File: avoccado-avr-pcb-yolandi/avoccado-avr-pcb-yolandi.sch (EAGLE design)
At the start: 55 parts, among them Q1 16MHz, Q2 FET, U2 MCP73831

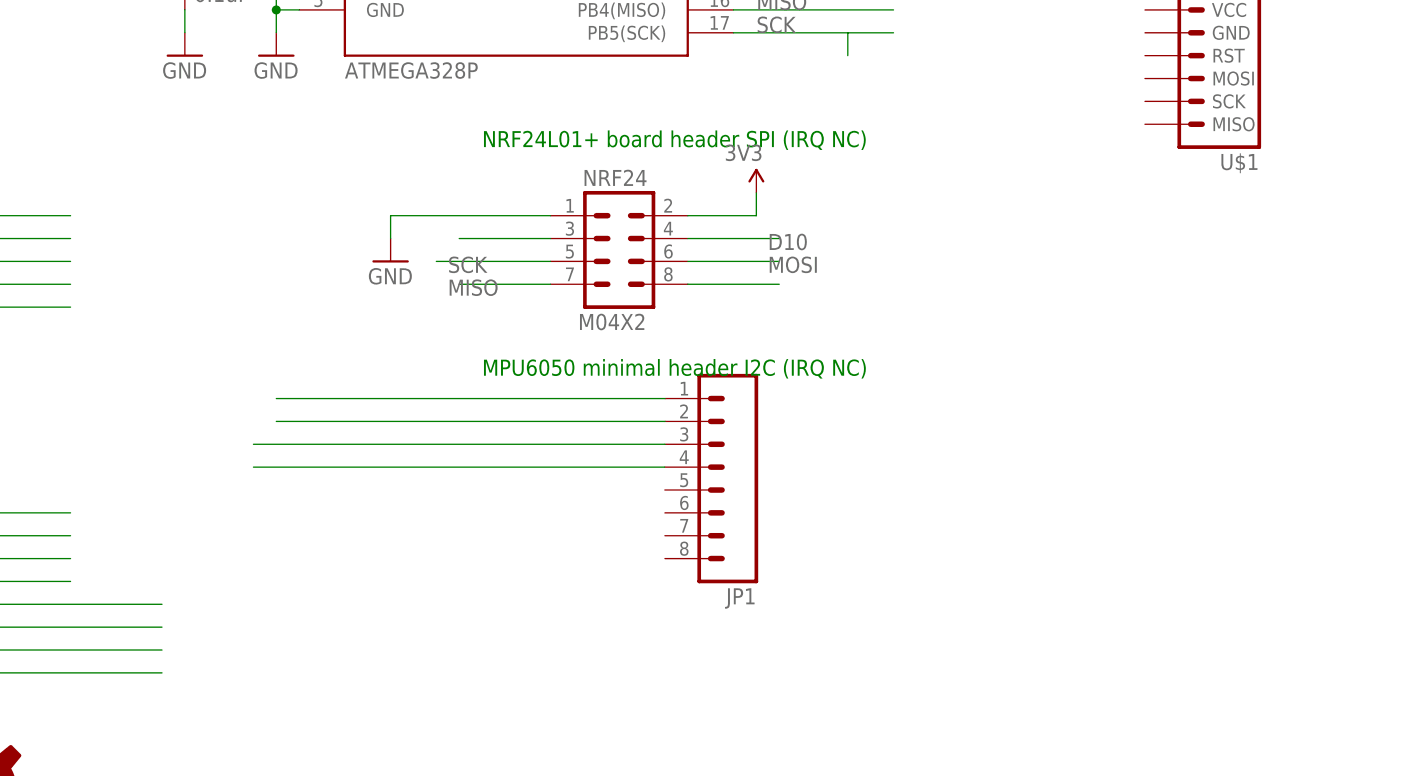
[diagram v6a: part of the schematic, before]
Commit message: change pkg of NRF24 header to round pins
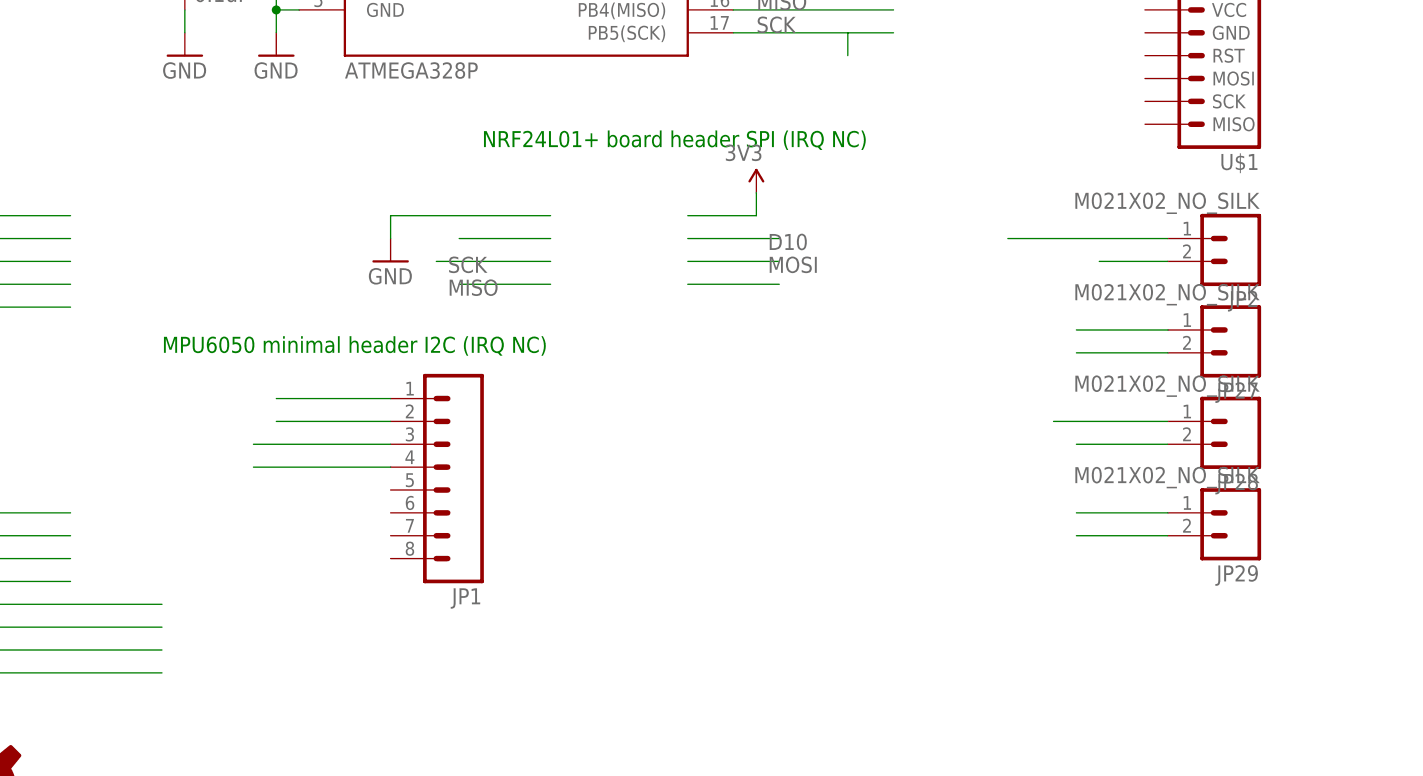
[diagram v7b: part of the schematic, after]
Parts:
- removed NRF24: M04X2, SparkFun-Connectors:M04X2
- added JP2, JP27, JP28, JP29: M021X02_NO_SILK, SparkFun-Connectors:M021X02_NO_SILK
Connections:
- net 3V3: now also JP2.2; no longer NRF24.2
- net A7: now also JP29.2; no longer NRF24.8
- net D10: now also JP27.2; no longer NRF24.4
- net D9: now also JP27.1; no longer NRF24.3
- net GND: now also JP2.1; no longer NRF24.1
- net MISO: now also JP29.1; no longer NRF24.7
- net MOSI: now also JP28.2; no longer NRF24.6
- net SCK: now also JP28.1; no longer NRF24.5
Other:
- moved on the sheet: JP1
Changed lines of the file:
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@@
 <part name="GND9" library="SparkFun" deviceset="GND" device=""/>
 <part name="R5" library="SparkFun-Resistors" deviceset="RESISTOR" device="0603" value="1M"/>
-<part name="NRF24" library="SparkFun-Connectors" deviceset="M04X2" device=""/>
 <part name="GND10" library="SparkFun" deviceset="GND" device=""/>
 <part name="P+2" library="SparkFun" deviceset="3.3V" device="" value="3V3"/>
@@
 <part name="JP25" library="SparkFun-Connectors" deviceset="M01" device="POGOPIN_HOLE_0.58"/>
 <part name="JP26" library="SparkFun-Connectors" deviceset="M01" device="POGOPIN_HOLE_0.58"/>
+<part name="JP2" library="SparkFun-Connectors" deviceset="M02" device="1X02_NO_SILK"/>
+<part name="JP27" library="SparkFun-Connectors" deviceset="M02" device="1X02_NO_SILK"/>
+<part name="JP28" library="SparkFun-Connectors" deviceset="M02" device="1X02_NO_SILK"/>
+<part name="JP29" library="SparkFun-Connectors" deviceset="M02" device="1X02_NO_SILK"/>
 </parts>
 <sheets>
@@
 <plain>
 <text x="187.96" y="83.82" size="1.778" layer="91">NRF24L01+ board header SPI (IRQ NC)</text>
-<text x="187.96" y="58.42" size="1.778" layer="91">MPU6050 minimal header I2C (IRQ NC)</text>
+<text x="152.4" y="60.96" size="1.778" layer="91">MPU6050 minimal header I2C (IRQ NC)</text>
 <text x="175.26" y="162.56" size="1.778" layer="91">AtMega 328p</text>
 <text x="33.02" y="175.26" size="1.778" layer="91">LiPo 1c charge IC</text>
@@
 <instance part="GND9" gate="1" x="55.88" y="63.5"/>
 <instance part="R5" gate="G$1" x="45.72" y="76.2" rot="R90"/>
-<instance part="NRF24" gate="G$1" x="203.2" y="71.12"/>
 <instance part="GND10" gate="1" x="177.8" y="71.12"/>
 <instance part="P+2" gate="G$1" x="218.44" y="78.74" smashed="yes">
 <attribute name="VALUE" x="214.884" y="82.296" size="1.778" layer="96"/>
 </instance>
-<instance part="JP1" gate="G$1" x="213.36" y="48.26" rot="R180"/>
+<instance part="JP1" gate="G$1" x="182.88" y="48.26" rot="R180"/>
 <instance part="R6" gate="G$1" x="48.26" y="137.16" rot="R90"/>
 <instance part="JP4" gate="G$1" x="238.76" y="137.16" rot="R180"/>
@@
 <instance part="JP25" gate="G$1" x="-10.16" y="-25.4" rot="R180"/>
 <instance part="JP26" gate="G$1" x="-10.16" y="-45.72" rot="R180"/>
+<instance part="JP2" gate="G$1" x="271.78" y="73.66" rot="R180"/>
+<instance part="JP27" gate="G$1" x="271.78" y="63.5" rot="R180"/>
+<instance part="JP28" gate="G$1" x="271.78" y="53.34" rot="R180"/>
+<instance part="JP29" gate="G$1" x="271.78" y="43.18" rot="R180"/>
 </instances>
 <busses>
@@
 </segment>
 <segment>
-<pinref part="NRF24" gate="G$1" pin="1"/>
 <wire x1="195.58" y1="76.2" x2="177.8" y2="76.2" width="0.2032" layer="91"/>
 <pinref part="GND10" gate="1" pin="GND"/>
@@
 </segment>
 <segment>
-<wire x1="208.28" y1="53.34" x2="165.1" y2="53.34" width="0.1524" layer="91"/>
+<wire x1="177.8" y1="53.34" x2="165.1" y2="53.34" width="0.1524" layer="91"/>
 <pinref part="JP1" gate="G$1" pin="2"/>
 </segment>
@@
 <pinref part="GND6" gate="1" pin="GND"/>
 <wire x1="35.56" y1="137.16" x2="35.56" y2="129.54" width="0.1524" layer="91"/>
+</segment>
+<segment>
+<wire x1="264.16" y1="73.66" x2="246.38" y2="73.66" width="0.2032" layer="91"/>
+<pinref part="JP2" gate="G$1" pin="1"/>
 </segment>
 </net>
@@
 <segment>
 <wire x1="182.88" y1="71.12" x2="195.58" y2="71.12" width="0.1524" layer="91"/>
-<pinref part="NRF24" gate="G$1" pin="5"/>
 <label x="184.15" y="69.85" size="1.778" layer="95"/>
 </segment>
@@
 <wire x1="142.24" y1="73.66" x2="116.84" y2="73.66" width="0.1524" layer="91"/>
 <pinref part="JP13" gate="G$1" pin="1"/>
+</segment>
+<segment>
+<wire x1="251.46" y1="53.34" x2="264.16" y2="53.34" width="0.1524" layer="91"/>
+<pinref part="JP28" gate="G$1" pin="1"/>
 </segment>
 </net>
@@
 <segment>
 <wire x1="185.42" y1="68.58" x2="195.58" y2="68.58" width="0.1524" layer="91"/>
-<pinref part="NRF24" gate="G$1" pin="7"/>
 <label x="184.15" y="67.31" size="1.778" layer="95"/>
 </segment>
@@
 <wire x1="142.24" y1="76.2" x2="116.84" y2="76.2" width="0.1524" layer="91"/>
 <pinref part="JP12" gate="G$1" pin="1"/>
+</segment>
+<segment>
+<wire x1="254" y1="43.18" x2="264.16" y2="43.18" width="0.1524" layer="91"/>
+<pinref part="JP29" gate="G$1" pin="1"/>
 </segment>
 </net>
@@
 <segment>
 <wire x1="210.82" y1="71.12" x2="220.98" y2="71.12" width="0.1524" layer="91"/>
-<pinref part="NRF24" gate="G$1" pin="6"/>
 <label x="219.71" y="69.85" size="1.778" layer="95"/>
 </segment>
@@
 <wire x1="142.24" y1="71.12" x2="116.84" y2="71.12" width="0.1524" layer="91"/>
 <pinref part="JP14" gate="G$1" pin="1"/>
+</segment>
+<segment>
+<wire x1="254" y1="50.8" x2="264.16" y2="50.8" width="0.1524" layer="91"/>
+<pinref part="JP28" gate="G$1" pin="2"/>
 </segment>
 </net>
@@
 <pinref part="P+2" gate="G$1" pin="3.3V"/>
 <wire x1="218.44" y1="78.74" x2="218.44" y2="76.2" width="0.2032" layer="91"/>
-<pinref part="NRF24" gate="G$1" pin="2"/>
 <wire x1="218.44" y1="76.2" x2="210.82" y2="76.2" width="0.2032" layer="91"/>
 </segment>
 <segment>
-<wire x1="208.28" y1="55.88" x2="165.1" y2="55.88" width="0.1524" layer="91"/>
+<wire x1="177.8" y1="55.88" x2="165.1" y2="55.88" width="0.1524" layer="91"/>
 <pinref part="JP1" gate="G$1" pin="1"/>
 </segment>
@@
 <label x="-43.18" y="-10.16" size="1.778" layer="95"/>
 </segment>
+<segment>
+<wire x1="264.16" y1="71.12" x2="256.54" y2="71.12" width="0.2032" layer="91"/>
+<pinref part="JP2" gate="G$1" pin="2"/>
+</segment>
 </net>
 <net name="D9" class="0">
@@
 <segment>
 <wire x1="185.42" y1="73.66" x2="195.58" y2="73.66" width="0.1524" layer="91"/>
-<pinref part="NRF24" gate="G$1" pin="3"/>
+</segment>
+<segment>
+<wire x1="254" y1="63.5" x2="264.16" y2="63.5" width="0.1524" layer="91"/>
+<pinref part="JP27" gate="G$1" pin="1"/>
 </segment>
 </net>
@@
 </segment>
 <segment>
-<wire x1="162.56" y1="50.8" x2="208.28" y2="50.8" width="0.1524" layer="91"/>
+<wire x1="162.56" y1="50.8" x2="177.8" y2="50.8" width="0.1524" layer="91"/>
 <pinref part="JP1" gate="G$1" pin="3"/>
 </segment>
@@
 </segment>
 <segment>
-<wire x1="162.56" y1="48.26" x2="208.28" y2="48.26" width="0.1524" layer="91"/>
+<wire x1="162.56" y1="48.26" x2="177.8" y2="48.26" width="0.1524" layer="91"/>
 <pinref part="JP1" gate="G$1" pin="4"/>
 </segment>
@@
 <segment>
 <wire x1="210.82" y1="73.66" x2="220.98" y2="73.66" width="0.1524" layer="91"/>
-<pinref part="NRF24" gate="G$1" pin="4"/>
 <label x="219.71" y="72.39" size="1.778" layer="95"/>
+</segment>
+<segment>
+<wire x1="254" y1="60.96" x2="264.16" y2="60.96" width="0.1524" layer="91"/>
+<pinref part="JP27" gate="G$1" pin="2"/>
 </segment>
 </net>
@@
 <segment>
 <wire x1="210.82" y1="68.58" x2="220.98" y2="68.58" width="0.1524" layer="91"/>
-<pinref part="NRF24" gate="G$1" pin="8"/>
-</segment>
-</net>
+</segment>
+<segment>
+<wire x1="254" y1="40.64" x2="264.16" y2="40.64" width="0.1524" layer="91"/>
+<pinref part="JP29" gate="G$1" pin="2"/>
+</segment>
+</net>

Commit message: schematic cleanup
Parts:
- removed JP16, JP7: M01POGOPIN_HOLE_0.58, SparkFun-Connectors:M01POGOPIN_HOLE_0.58
- removed JP4: (no value), SparkFun-Connectors:M08NO_SILK
- removed JP5: M01SMD, SparkFun-Connectors:M01SMD
- removed TP2: TEST-POINT3X4, SparkFun-Passives:TEST-POINT3X4
- removed TP3: TEST-POINT3, SparkFun-Passives:TEST-POINT3
- removed TP4: TEST-POINT2, SparkFun-Passives:TEST-POINT2
- removed TP5: TEST-POINTTP_15TH_THRU, SparkFun-Passives:TEST-POINTTP_15TH_THRU
- removed U$1: AVR_MINI_PROGSMD, SparkFun-Connectors:AVR_MINI_PROGSMD
- JP1: value (none) -> MPU6050
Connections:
- net A7 renamed A7-NRF-IRQ
- removed net 3V3: AVR.AVCC, AVR.VCC@1, AVR.VCC@2, C10.1, C3.2, C6.1, JP1.1, JP11.1, JP16.1, JP18.1, JP2.2, LDO.VO, R2.2
- new net 3.3V: AVR.AVCC, AVR.VCC@1, AVR.VCC@2, C10.1, C3.2, C6.1, JP1.1, JP11.1, JP18.1, JP2.2, LDO.VO, R2.2
- net VBAT: no longer JP7.1
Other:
- moved on the sheet: JP10, JP11, JP17, JP18, JP2, JP23, JP24, JP25, JP26, JP27, JP28, JP29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
